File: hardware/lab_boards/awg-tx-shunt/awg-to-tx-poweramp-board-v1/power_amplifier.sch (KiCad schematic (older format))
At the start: 14 parts

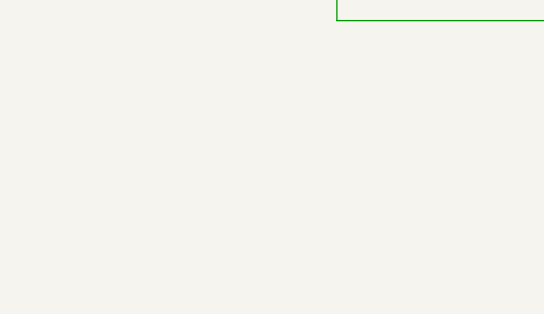
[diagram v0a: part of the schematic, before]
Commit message: Added some TTL logic controls for interfacing with either the USB DAQ or a custom MCU solution.
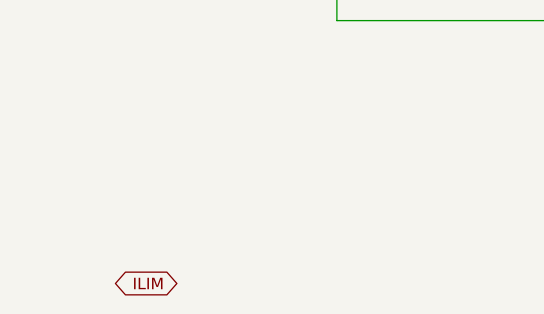
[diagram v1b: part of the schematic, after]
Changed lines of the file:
@@
 	3350 3850 3350 3650
 Connection ~ 3350 3650
+Text GLabel 1700 5350 0    50   BiDi ~ 0
+ILIM
 $EndSCHEMATC
